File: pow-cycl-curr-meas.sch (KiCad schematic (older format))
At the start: 41 parts

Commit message: Schematic complete
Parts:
- gave numbers to parts that had none: 41
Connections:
- no-connect marks 0 -> 6

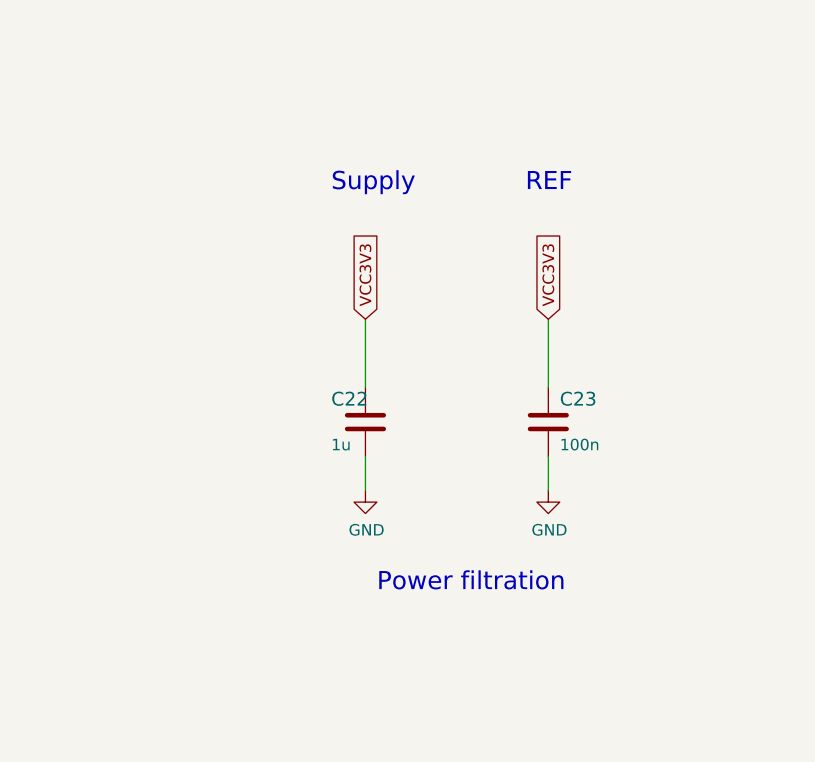
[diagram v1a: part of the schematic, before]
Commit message: PCB creation. Components gathered in functional groups
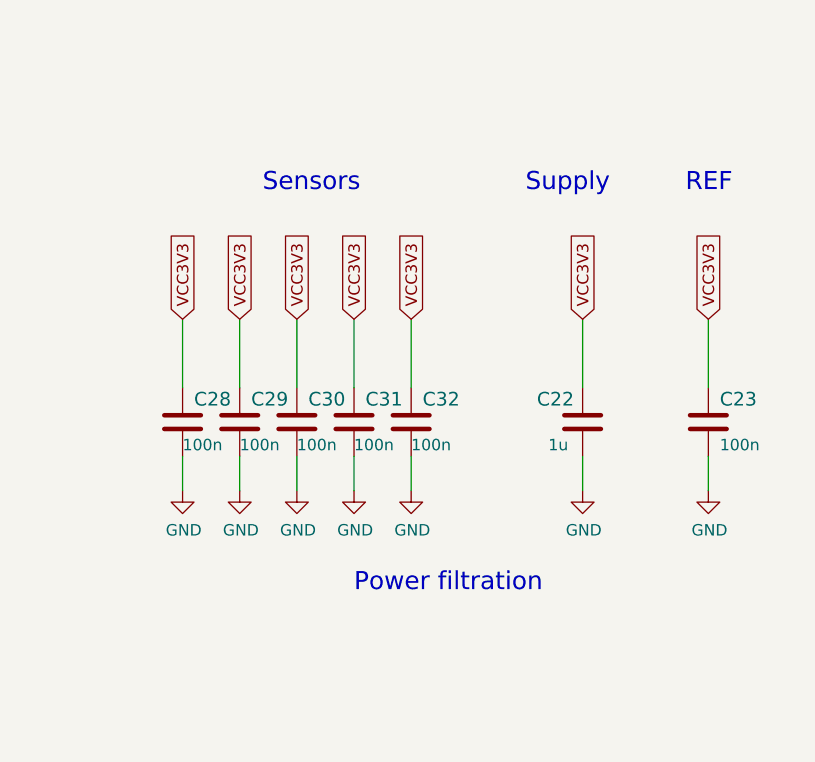
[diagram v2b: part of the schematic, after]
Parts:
- added C28, C29, C30, C31, C32: C_100n_0402, antmicro-footprints:0402-cap, symbol antmicroCapacitors0402:C_100n_0402
- U10: footprint (none) -> antmicro-footprints:TSSOP-16; Manufacturer (none) -> Texas Instruments
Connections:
- net GND: now also C28.2, C29.2, C30.2, C31.2, C32.2
- net VCC3V3: now also C28.1, C29.1, C30.1, C31.1, C32.1
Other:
- note added: "Sensors\n"
- moved on the sheet: C22, C23
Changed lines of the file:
@@
 F 0 "U10" H 3000 7950 50  0000 C CNN
 F 1 "TCA9534" H 3000 7850 50  0000 C CNN
-F 2 "" H 4250 6750 50  0001 C CNN
+F 2 "antmicro-footprints:TSSOP-16" H 4250 6750 50  0001 C CNN
 F 3 "http://www.ti.com/lit/ds/symlink/tca9534.pdf" H 3400 7200 50  0001 C CNN
 F 4 "TCA9534ADWR" H 3300 7300 50  0001 C CNN "MPN"
-F 5 "Texas Instruments" H 3300 7300 50  0001 C CNN "Manufaacturer"
+F 5 "Texas Instruments" H 3300 7300 50  0001 C CNN "Manufacturer"
+F 6 "Texas Instruments" H 3300 7300 50  0001 C CNN "Manufaacturer"
 	1    3300 7300
 	1    0    0    -1
@@
 L antmicroCapacitors0402:C_100n_0402 C23
 U 1 1 6269F66B
-P 14900 2650
-F 0 "C23" H 14950 2750 60  0000 L CNN
-F 1 "C_100n_0402" H 14900 2500 60  0001 C CNN
-F 2 "antmicro-footprints:0402-cap" H 15100 2850 60  0001 L CNN
-F 3 "" H 14900 2650 50  0001 C CNN
-F 4 "Murata" H 15100 3050 60  0001 L CNN "Manufacturer"
-F 5 "GRM155R61H104KE14D" H 15100 2950 60  0001 L CNN "MPN"
-F 6 "100n" H 14950 2550 50  0000 L CNN "Val"
-	1    14900 2650
+P 15600 2650
+F 0 "C23" H 15650 2750 60  0000 L CNN
+F 1 "C_100n_0402" H 15600 2500 60  0001 C CNN
+F 2 "antmicro-footprints:0402-cap" H 15800 2850 60  0001 L CNN
+F 3 "" H 15600 2650 50  0001 C CNN
+F 4 "Murata" H 15800 3050 60  0001 L CNN "Manufacturer"
+F 5 "GRM155R61H104KE14D" H 15800 2950 60  0001 L CNN "MPN"
+F 6 "100n" H 15650 2550 50  0000 L CNN "Val"
+	1    15600 2650
 	1    0    0    -1
 $EndComp
@@
 L antmicroCapacitors0402:C_1u_0402 C22
 U 1 1 626A4815
-P 14100 2650
-F 0 "C22" H 13950 2750 60  0000 L CNN
-F 1 "C_1u_0402" H 14100 2500 60  0001 C CNN
-F 2 "antmicro-footprints:0402-cap" H 14300 2850 60  0001 L CNN
-F 3 "" H 14100 2650 50  0001 C CNN
-F 4 "TDK" H 14300 3050 60  0001 L CNN "Manufacturer"
-F 5 "C1005X6S1A105K050BC" H 14300 2950 60  0001 L CNN "MPN"
-F 6 "1u" H 13950 2550 50  0000 L CNN "Val"
-	1    14100 2650
+P 15050 2650
+F 0 "C22" H 14850 2750 60  0000 L CNN
+F 1 "C_1u_0402" H 15050 2500 60  0001 C CNN
+F 2 "antmicro-footprints:0402-cap" H 15250 2850 60  0001 L CNN
+F 3 "" H 15050 2650 50  0001 C CNN
+F 4 "TDK" H 15250 3050 60  0001 L CNN "Manufacturer"
+F 5 "C1005X6S1A105K050BC" H 15250 2950 60  0001 L CNN "MPN"
+F 6 "1u" H 14900 2550 50  0000 L CNN "Val"
+	1    15050 2650
 	1    0    0    -1
 $EndComp
@@
 L power:GND #PWR059
 U 1 1 626A4C27
-P 14100 2950
-F 0 "#PWR059" H 14100 2700 50  0001 C CNN
-F 1 "GND" H 14105 2777 50  0000 C CNN
-F 2 "" H 14100 2950 50  0001 C CNN
-F 3 "" H 14100 2950 50  0001 C CNN
-	1    14100 2950
+P 15050 2950
+F 0 "#PWR059" H 15050 2700 50  0001 C CNN
+F 1 "GND" H 15055 2777 50  0000 C CNN
+F 2 "" H 15050 2950 50  0001 C CNN
+F 3 "" H 15050 2950 50  0001 C CNN
+	1    15050 2950
 	1    0    0    -1
 $EndComp
@@
 L power:GND #PWR060
 U 1 1 626A4F78
-P 14900 2950
-F 0 "#PWR060" H 14900 2700 50  0001 C CNN
-F 1 "GND" H 14905 2777 50  0000 C CNN
-F 2 "" H 14900 2950 50  0001 C CNN
-F 3 "" H 14900 2950 50  0001 C CNN
-	1    14900 2950
+P 15600 2950
+F 0 "#PWR060" H 15600 2700 50  0001 C CNN
+F 1 "GND" H 15605 2777 50  0000 C CNN
+F 2 "" H 15600 2950 50  0001 C CNN
+F 3 "" H 15600 2950 50  0001 C CNN
+	1    15600 2950
 	1    0    0    -1
 $EndComp
 Wire Wire Line
-	14100 2950 14100 2800
+	15050 2950 15050 2800
 Wire Wire Line
-	14900 2950 14900 2800
+	15600 2950 15600 2800
 $Comp
 L antmicroCapacitors0402:C_100n_0402 C21
@@
 Wire Wire Line
 	5650 8050 5650 8200
-Text Notes 14800 1650 0    79   ~ 0
+Text Notes 15500 1650 0    79   ~ 0
 REF
-Text Notes 13950 1650 0    79   ~ 0
+Text Notes 14800 1650 0    79   ~ 0
 Supply\n
 $Comp
@@
 EndData
 $EndBitmap
-Text Notes 14150 3400 0    79   ~ 0
+Text Notes 14050 3400 0    79   ~ 0
 Power filtration
 Text Notes 12900 7900 0    79   ~ 0
@@
 Text Notes 2050 4900 0    59   ~ 0
 To perform more accurate measurement, the sensor can be replaced\nwith *A3 part (MPN: TMCS1100A3-Q1). Note that it will result in\n measured currents range reduction (to up to 15.5A unidirect.).
-Text GLabel 14100 2200 1    50   Input ~ 0
+Text GLabel 15050 2200 1    50   Input ~ 0
 VCC3V3
-Text GLabel 14900 2200 1    50   Input ~ 0
+Text GLabel 15600 2200 1    50   Input ~ 0
 VCC3V3
 Wire Wire Line
-	14100 2200 14100 2500
+	15050 2200 15050 2500
 Wire Wire Line
-	14900 2200 14900 2500
+	15600 2200 15600 2500
 $Bitmap
 Pos 1450 10900
@@
 NoConn ~ 10400 2850
 NoConn ~ 10400 2750
+Text GLabel 13300 2200 1    50   Input ~ 0
+VCC3V3
+Text GLabel 13550 2200 1    50   Input ~ 0
+VCC3V3
+Text GLabel 13800 2200 1    50   Input ~ 0
+VCC3V3
+Text GLabel 14050 2200 1    50   Input ~ 0
+VCC3V3
+Text GLabel 14300 2200 1    50   Input ~ 0
+VCC3V3
+$Comp
+L antmicroCapacitors0402:C_100n_0402 C28
+U 1 1 6253CB8D
+P 13300 2650
+F 0 "C28" H 13350 2750 60  0000 L CNN
+F 1 "C_100n_0402" H 13300 2500 60  0001 C CNN
+F 2 "antmicro-footprints:0402-cap" H 13500 2850 60  0001 L CNN
+F 3 "" H 13300 2650 50  0001 C CNN
+F 4 "Murata" H 13500 3050 60  0001 L CNN "Manufacturer"
+F 5 "GRM155R61H104KE14D" H 13500 2950 60  0001 L CNN "MPN"
+F 6 "100n" H 13300 2550 50  0000 L CNN "Val"
+	1    13300 2650
+	1    0    0    -1
+$EndComp
+$Comp
+L antmicroCapacitors0402:C_100n_0402 C29
+U 1 1 6253D002
+P 13550 2650
+F 0 "C29" H 13600 2750 60  0000 L CNN
+F 1 "C_100n_0402" H 13550 2500 60  0001 C CNN
+F 2 "antmicro-footprints:0402-cap" H 13750 2850 60  0001 L CNN
+F 3 "" H 13550 2650 50  0001 C CNN
+F 4 "Murata" H 13750 3050 60  0001 L CNN "Manufacturer"
+F 5 "GRM155R61H104KE14D" H 13750 2950 60  0001 L CNN "MPN"
+F 6 "100n" H 13550 2550 50  0000 L CNN "Val"
+	1    13550 2650
+	1    0    0    -1
+$EndComp
+$Comp
+L antmicroCapacitors0402:C_100n_0402 C30
+U 1 1 6253D621
+P 13800 2650
+F 0 "C30" H 13850 2750 60  0000 L CNN
+F 1 "C_100n_0402" H 13800 2500 60  0001 C CNN
+F 2 "antmicro-footprints:0402-cap" H 14000 2850 60  0001 L CNN
+F 3 "" H 13800 2650 50  0001 C CNN
+F 4 "Murata" H 14000 3050 60  0001 L CNN "Manufacturer"
+F 5 "GRM155R61H104KE14D" H 14000 2950 60  0001 L CNN "MPN"
+F 6 "100n" H 13800 2550 50  0000 L CNN "Val"
+	1    13800 2650
+	1    0    0    -1
+$EndComp
+$Comp
+L antmicroCapacitors0402:C_100n_0402 C31
+U 1 1 6253D9BA
+P 14050 2650
+F 0 "C31" H 14100 2750 60  0000 L CNN
+F 1 "C_100n_0402" H 14050 2500 60  0001 C CNN
+F 2 "antmicro-footprints:0402-cap" H 14250 2850 60  0001 L CNN
+F 3 "" H 14050 2650 50  0001 C CNN
+F 4 "Murata" H 14250 3050 60  0001 L CNN "Manufacturer"
+F 5 "GRM155R61H104KE14D" H 14250 2950 60  0001 L CNN "MPN"
+F 6 "100n" H 14050 2550 50  0000 L CNN "Val"
+	1    14050 2650
+	1    0    0    -1
+$EndComp
+$Comp
+L antmicroCapacitors0402:C_100n_0402 C32
+U 1 1 6253DCAF
+P 14300 2650
+F 0 "C32" H 14350 2750 60  0000 L CNN
+F 1 "C_100n_0402" H 14300 2500 60  0001 C CNN
+F 2 "antmicro-footprints:0402-cap" H 14500 2850 60  0001 L CNN
+F 3 "" H 14300 2650 50  0001 C CNN
+F 4 "Murata" H 14500 3050 60  0001 L CNN "Manufacturer"
+F 5 "GRM155R61H104KE14D" H 14500 2950 60  0001 L CNN "MPN"
+F 6 "100n" H 14300 2550 50  0000 L CNN "Val"
+	1    14300 2650
+	1    0    0    -1
+$EndComp
+$Comp
+L power:GND #PWR070
+U 1 1 6256CD61
+P 14300 2950
+F 0 "#PWR070" H 14300 2700 50  0001 C CNN
+F 1 "GND" H 14305 2777 50  0000 C CNN
+F 2 "" H 14300 2950 50  0001 C CNN
+F 3 "" H 14300 2950 50  0001 C CNN
+	1    14300 2950
+	1    0    0    -1
+$EndComp
+$Comp
+L power:GND #PWR069
+U 1 1 6256D20A
+P 14050 2950
+F 0 "#PWR069" H 14050 2700 50  0001 C CNN
+F 1 "GND" H 14055 2777 50  0000 C CNN
+F 2 "" H 14050 2950 50  0001 C CNN
+F 3 "" H 14050 2950 50  0001 C CNN
+	1    14050 2950
+	1    0    0    -1
+$EndComp
+$Comp
+L power:GND #PWR068
+U 1 1 6256D538
+P 13800 2950
+F 0 "#PWR068" H 13800 2700 50  0001 C CNN
+F 1 "GND" H 13805 2777 50  0000 C CNN
+F 2 "" H 13800 2950 50  0001 C CNN
+F 3 "" H 13800 2950 50  0001 C CNN
+	1    13800 2950
+	1    0    0    -1
+$EndComp
+$Comp
+L power:GND #PWR067
+U 1 1 6256D868
+P 13550 2950
+F 0 "#PWR067" H 13550 2700 50  0001 C CNN
+F 1 "GND" H 13555 2777 50  0000 C CNN
+F 2 "" H 13550 2950 50  0001 C CNN
+F 3 "" H 13550 2950 50  0001 C CNN
+	1    13550 2950
+	1    0    0    -1
+$EndComp
+$Comp
+L power:GND #PWR025
+U 1 1 6256DBAC
+P 13300 2950
+F 0 "#PWR025" H 13300 2700 50  0001 C CNN
+F 1 "GND" H 13305 2777 50  0000 C CNN
+F 2 "" H 13300 2950 50  0001 C CNN
+F 3 "" H 13300 2950 50  0001 C CNN
+	1    13300 2950
+	1    0    0    -1
+$EndComp
+Wire Wire Line
+	13300 2200 13300 2500
+Wire Wire Line
+	13550 2200 13550 2500
+Wire Wire Line
+	13800 2500 13800 2200
+Wire Wire Line
+	14050 2200 14050 2500
+Wire Wire Line
+	14300 2200 14300 2500
+Wire Wire Line
+	13300 2950 13300 2800
+Wire Wire Line
+	13550 2950 13550 2800
+Wire Wire Line
+	13800 2950 13800 2800
+Wire Wire Line
+	14050 2950 14050 2800
+Wire Wire Line
+	14300 2800 14300 2950
+Text Notes 13650 1650 0    79   ~ 0
+Sensors\n
 $EndSCHEMATC

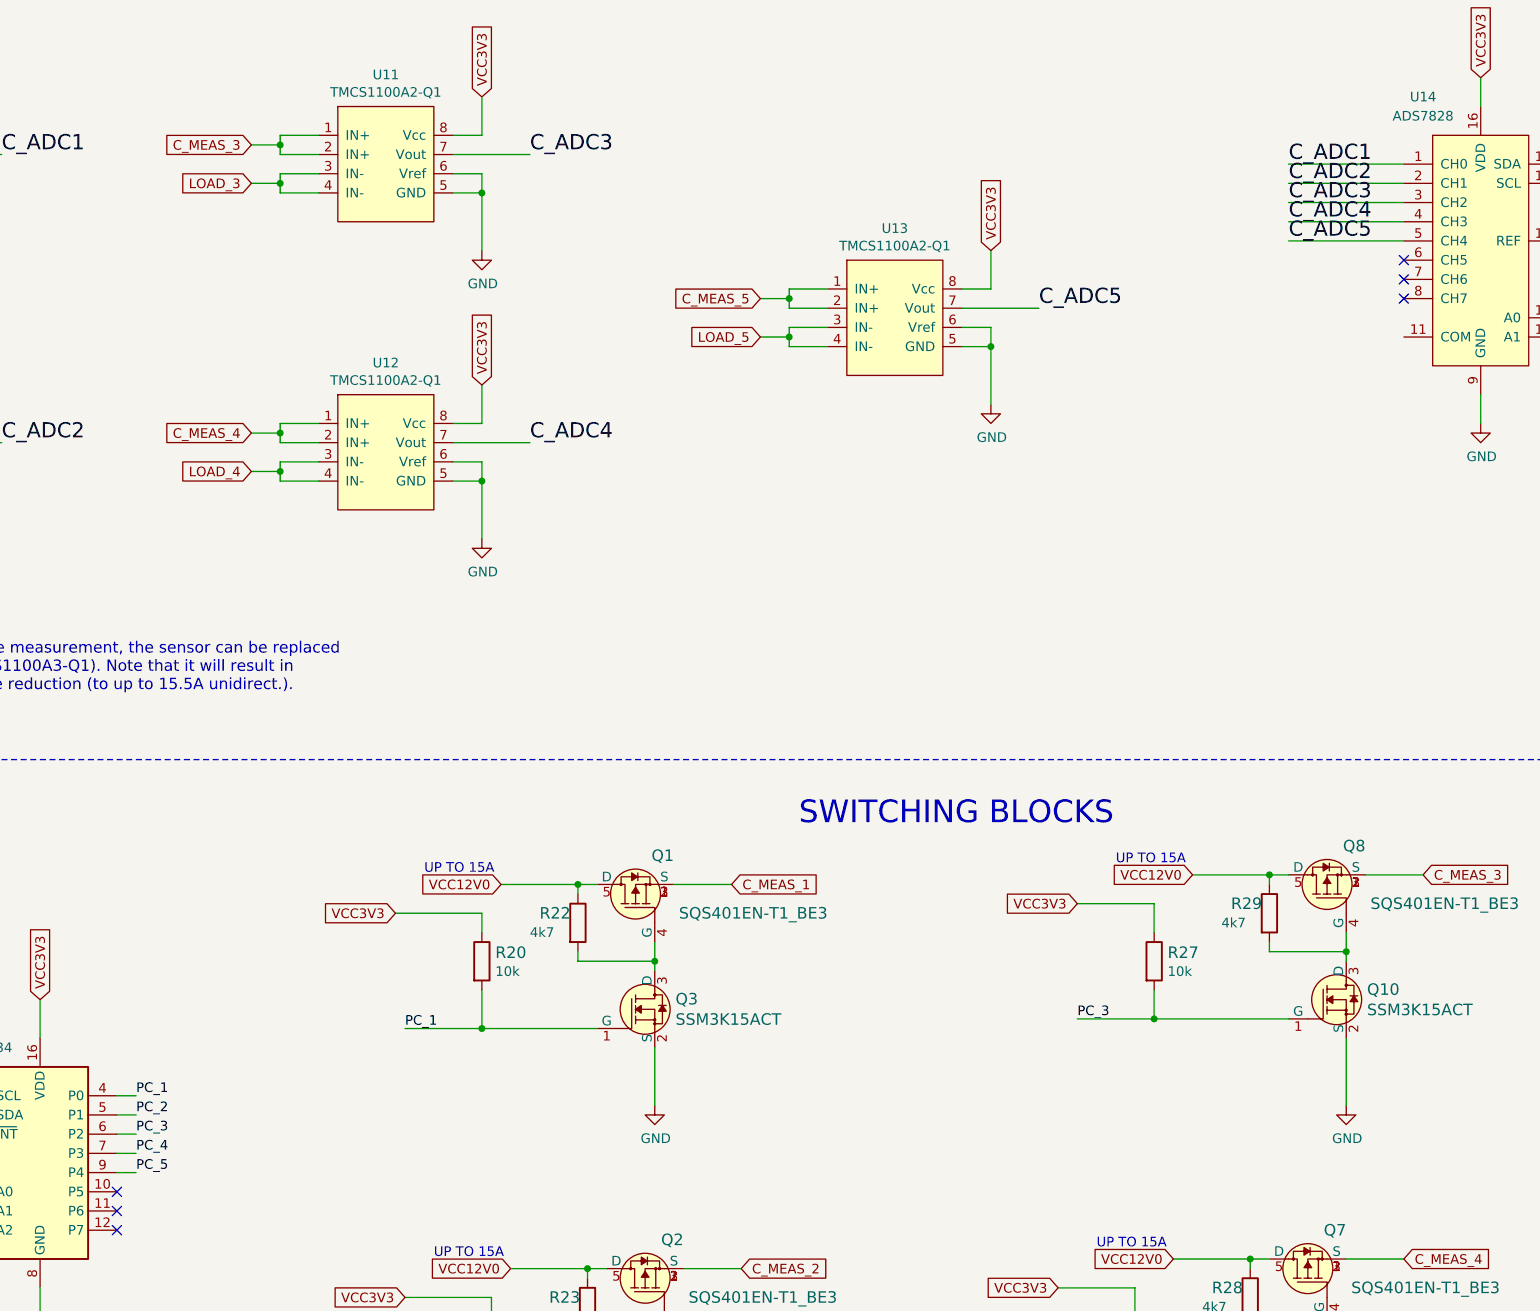
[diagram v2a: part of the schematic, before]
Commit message: Initial component placement done
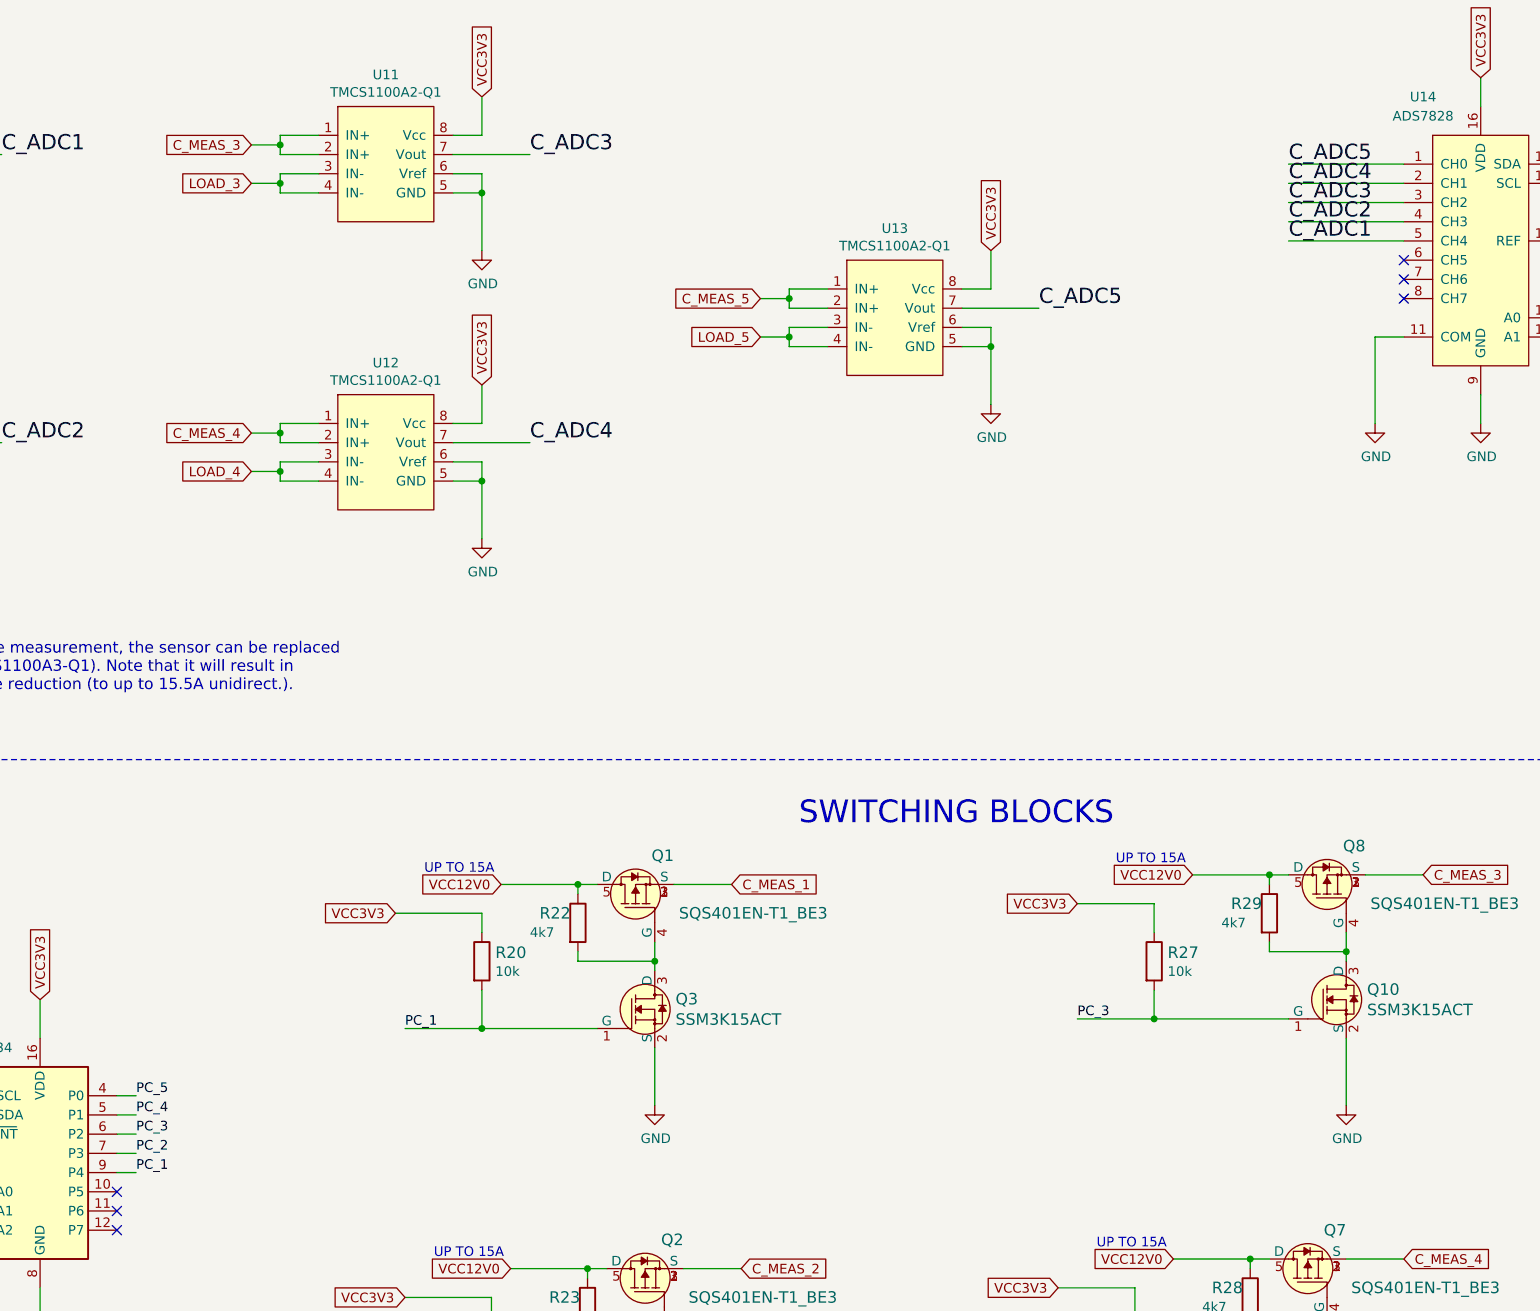
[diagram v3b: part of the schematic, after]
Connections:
- net C_ADC1: now also U14.5 (CH4); no longer U14.1 (CH0)
- net C_ADC2: now also U14.4 (CH3); no longer U14.2 (CH1)
- net C_ADC4: now also U14.2 (CH1); no longer U14.4 (CH3)
- net C_ADC5: now also U14.1 (CH0); no longer U14.5 (CH4)
- net GND: now also U14.11 (COM)
- net PC_1: now also U10.9 (P4); no longer U10.4 (P0)
- net PC_2: now also U10.7 (P3); no longer U10.5 (P1)
- net PC_4: now also U10.5 (P1); no longer U10.7 (P3)
- net PC_5: now also U10.4 (P0); no longer U10.9 (P4)
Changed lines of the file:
@@
 	3300 8300 3300 8000
 Text Label 3800 7000 0    50   ~ 0
-PC_1
+PC_5
 Text Label 3800 7100 0    50   ~ 0
-PC_2
+PC_4
 Text Label 3800 7200 0    50   ~ 0
 PC_3
 Text Label 3800 7300 0    50   ~ 0
-PC_4
+PC_2
 Text Label 3800 7400 0    50   ~ 0
-PC_5
+PC_1
 Text Label 8700 6600 0    50   ~ 0
 PC_3
@@
 	10800 1850 10800 1700
 Text Label 9800 2150 0    79   ~ 0
-C_ADC1
+C_ADC5
 Text Label 9800 2250 0    79   ~ 0
-C_ADC2
+C_ADC4
 Text Label 9800 2350 0    79   ~ 0
 C_ADC3
 Text Label 9800 2450 0    79   ~ 0
-C_ADC4
+C_ADC2
 Text Label 9800 2550 0    79   ~ 0
-C_ADC5
+C_ADC1
 Wire Wire Line
 	10400 2150 9800 2150
@@
 Text Notes 13650 1650 0    79   ~ 0
 Sensors\n
+$Comp
+L power:GND #PWR0101
+U 1 1 627158BA
+P 10250 3500
+F 0 "#PWR0101" H 10250 3250 50  0001 C CNN
+F 1 "GND" H 10255 3327 50  0000 C CNN
+F 2 "" H 10250 3500 50  0001 C CNN
+F 3 "" H 10250 3500 50  0001 C CNN
+	1    10250 3500
+	1    0    0    -1
+$EndComp
+Wire Wire Line
+	10250 3500 10250 3050
+Wire Wire Line
+	10250 3050 10400 3050
 $EndSCHEMATC
